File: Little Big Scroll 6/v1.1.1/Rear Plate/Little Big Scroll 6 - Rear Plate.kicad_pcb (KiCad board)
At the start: 2 copper layers, 59.2 x 87 mm, 6 parts

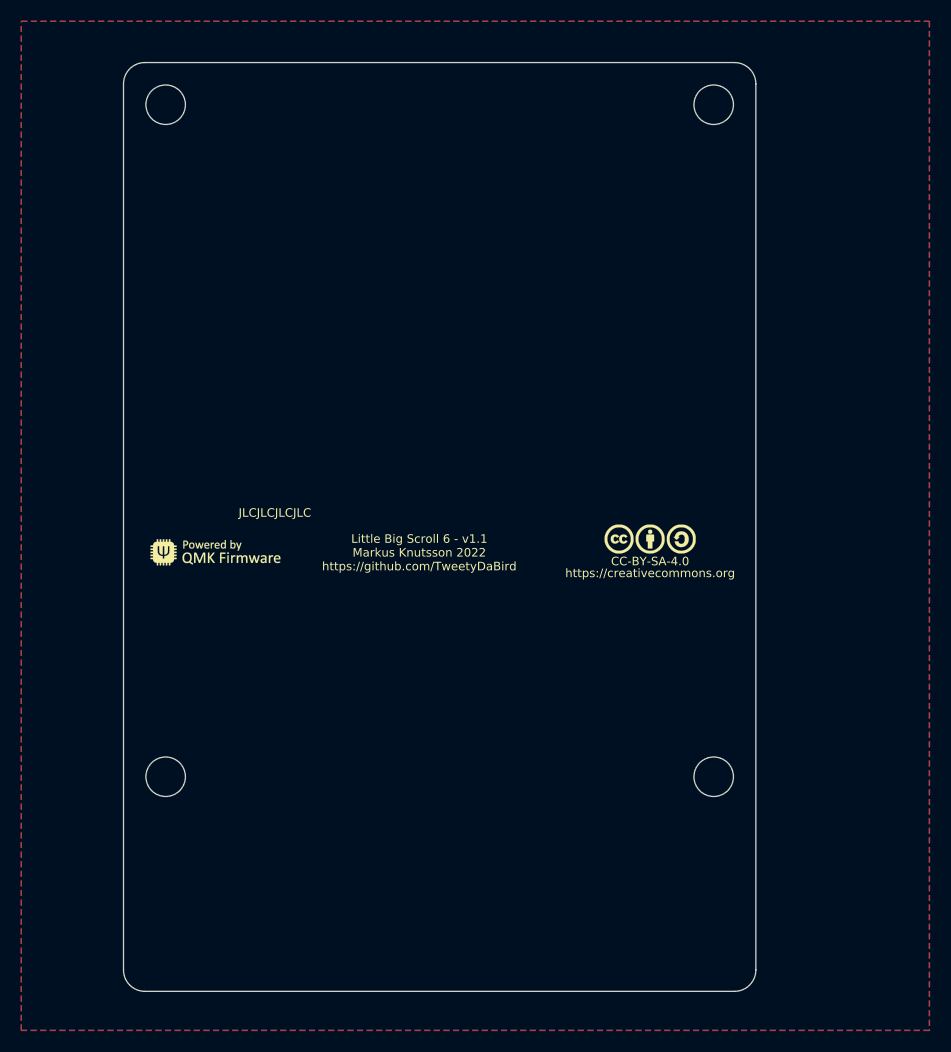
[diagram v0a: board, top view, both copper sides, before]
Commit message: LBS6 v1.1.1
Fixed plate holes
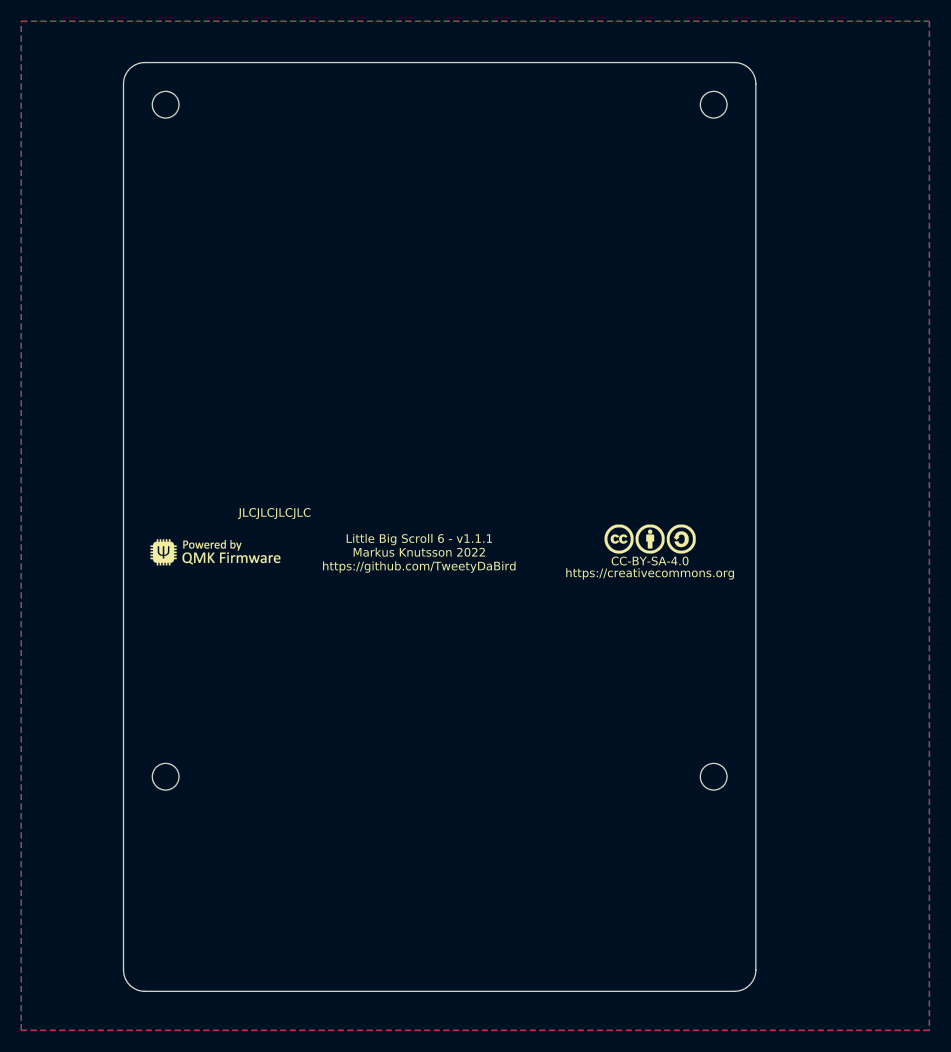
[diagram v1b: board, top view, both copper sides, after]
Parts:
- H1, H2, H3, H4: footprint Keyboard Switches & Encoders:Spacer PCB hole -> Keyboard_Plate:Spacer Plate hole
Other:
- board text added: "Little Big Scroll 6 - v1.1.1 Markus Knutsson 2022 https://github.com/TweetyDaBird"
- board text removed: "Little Big Scroll 6 - v1.1 Markus Knutsson 2022 https://github.com/TweetyDaBird"
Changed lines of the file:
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@@
   (title_block
     (title "Little Big Scroll 6 - Rear Plate")
-    (date "2022-08-26")
-    (rev "v1.1")
+    (date "2022-09-16")
+    (rev "v1.1.1")
     (company "Tweety's Wild Thinking")
     (comment 1 "Markus Knutsson <markus.knutsson@tweety.se>")
@@
   )
   (net 0 "")
-  (footprint "Keyboard Switches & Encoders:Spacer PCB hole" (layer "F.Cu")
+  (footprint "Keyboard_Plate:Spacer Plate hole" (layer "F.Cu")
     (at 84.6 112.685)
-    (descr "Mounting Hole 3.7mm, no annular")
-    (tags "mounting hole 3.7mm no annular")
+    (descr "Mounting Hole 2.5mm, no annular")
+    (tags "mounting hole 2.5mm no annular")
     (property "Sheetfile" "Little Big Scroll 6 - Rear Plate.kicad_sch")
     (property "Sheetname" "")
     (attr exclude_from_pos_files)
-    (fp_text reference "H1" (at 0 -4.7) (layer "F.SilkS") hide
+    (fp_text reference "H1" (at 0 -3.5) (layer "F.SilkS") hide
       (effects (font (size 1 1) (thickness 0.15)))
     )
-    (fp_text value "Spacer_PCB" (at 0 4.7) (layer "F.Fab") hide
+    (fp_text value "Spacer_PCB" (at 0 3.5) (layer "F.Fab")
       (effects (font (size 1 1) (thickness 0.15)))
     )
-    (fp_text user "${REFERENCE}" (at 0 0) (layer "F.Fab") hide
+    (fp_text user "${REFERENCE}" (at 0 0) (layer "F.Fab")
       (effects (font (size 1 1) (thickness 0.15)))
     )
-    (fp_circle (center 0 0) (end 3.7 0) (layer "Cmts.User") (width 0.15) (fill none))
-    (fp_circle (center 0 0) (end 3.95 0) (layer "F.CrtYd") (width 0.05) (fill none))
-    (pad "" np_thru_hole circle (at 0 0) (size 3.7 3.7) (drill 3.7) (layers *.Cu *.Mask))
+    (fp_circle (center 0 0) (end 2.5 0) (layer "Cmts.User") (width 0.15) (fill none))
+    (fp_circle (center 0 0) (end 2.75 0) (layer "F.CrtYd") (width 0.05) (fill none))
+    (pad "" np_thru_hole circle (at 0 0) (size 2.5 2.5) (drill 2.5) (layers *.Cu *.Mask))
   )
-  (footprint "Keyboard Switches & Encoders:Spacer PCB hole" (layer "F.Cu")
+  (footprint "Keyboard_Plate:Spacer Plate hole" (layer "F.Cu")
     (at 135.94 112.685)
-    (descr "Mounting Hole 3.7mm, no annular")
-    (tags "mounting hole 3.7mm no annular")
+    (descr "Mounting Hole 2.5mm, no annular")
+    (tags "mounting hole 2.5mm no annular")
     (property "Sheetfile" "Little Big Scroll 6 - Rear Plate.kicad_sch")
     (property "Sheetname" "")
     (attr exclude_from_pos_files)
-    (fp_text reference "H2" (at 0 -4.7) (layer "F.SilkS") hide
+    (fp_text reference "H2" (at 0 -3.5) (layer "F.SilkS") hide
       (effects (font (size 1 1) (thickness 0.15)))
     )
-    (fp_text value "Spacer_PCB" (at 0 4.7) (layer "F.Fab") hide
+    (fp_text value "Spacer_PCB" (at 0 3.5) (layer "F.Fab")
       (effects (font (size 1 1) (thickness 0.15)))
     )
-    (fp_text user "${REFERENCE}" (at 0 0) (layer "F.Fab") hide
+    (fp_text user "${REFERENCE}" (at 0 0) (layer "F.Fab")
       (effects (font (size 1 1) (thickness 0.15)))
     )
-    (fp_circle (center 0 0) (end 3.7 0) (layer "Cmts.User") (width 0.15) (fill none))
-    (fp_circle (center 0 0) (end 3.95 0) (layer "F.CrtYd") (width 0.05) (fill none))
-    (pad "" np_thru_hole circle (at 0 0) (size 3.7 3.7) (drill 3.7) (layers *.Cu *.Mask))
+    (fp_circle (center 0 0) (end 2.5 0) (layer "Cmts.User") (width 0.15) (fill none))
+    (fp_circle (center 0 0) (end 2.75 0) (layer "F.CrtYd") (width 0.05) (fill none))
+    (pad "" np_thru_hole circle (at 0 0) (size 2.5 2.5) (drill 2.5) (layers *.Cu *.Mask))
   )
-  (footprint "Keyboard Switches & Encoders:Spacer PCB hole" (layer "F.Cu")
+  (footprint "Keyboard_Plate:Spacer Plate hole" (layer "F.Cu")
     (at 135.94 49.73)
-    (descr "Mounting Hole 3.7mm, no annular")
-    (tags "mounting hole 3.7mm no annular")
+    (descr "Mounting Hole 2.5mm, no annular")
+    (tags "mounting hole 2.5mm no annular")
     (property "Sheetfile" "Little Big Scroll 6 - Rear Plate.kicad_sch")
     (property "Sheetname" "")
     (attr exclude_from_pos_files)
-    (fp_text reference "H3" (at 0 -4.7) (layer "F.SilkS") hide
+    (fp_text reference "H3" (at 0 -3.5) (layer "F.SilkS") hide
       (effects (font (size 1 1) (thickness 0.15)))
     )
-    (fp_text value "Spacer_PCB" (at 0 4.7) (layer "F.Fab") hide
+    (fp_text value "Spacer_PCB" (at 0 3.5) (layer "F.Fab")
       (effects (font (size 1 1) (thickness 0.15)))
     )
-    (fp_text user "${REFERENCE}" (at 0 0) (layer "F.Fab") hide
+    (fp_text user "${REFERENCE}" (at 0 0) (layer "F.Fab")
       (effects (font (size 1 1) (thickness 0.15)))
     )
-    (fp_circle (center 0 0) (end 3.7 0) (layer "Cmts.User") (width 0.15) (fill none))
-    (fp_circle (center 0 0) (end 3.95 0) (layer "F.CrtYd") (width 0.05) (fill none))
-    (pad "" np_thru_hole circle (at 0 0) (size 3.7 3.7) (drill 3.7) (layers *.Cu *.Mask))
+    (fp_circle (center 0 0) (end 2.5 0) (layer "Cmts.User") (width 0.15) (fill none))
+    (fp_circle (center 0 0) (end 2.75 0) (layer "F.CrtYd") (width 0.05) (fill none))
+    (pad "" np_thru_hole circle (at 0 0) (size 2.5 2.5) (drill 2.5) (layers *.Cu *.Mask))
   )
-  (footprint "Keyboard Switches & Encoders:Spacer PCB hole" (layer "F.Cu")
+  (footprint "Keyboard_Plate:Spacer Plate hole" (layer "F.Cu")
     (at 84.6 49.73)
-    (descr "Mounting Hole 3.7mm, no annular")
-    (tags "mounting hole 3.7mm no annular")
+    (descr "Mounting Hole 2.5mm, no annular")
+    (tags "mounting hole 2.5mm no annular")
     (property "Sheetfile" "Little Big Scroll 6 - Rear Plate.kicad_sch")
     (property "Sheetname" "")
     (attr exclude_from_pos_files)
-    (fp_text reference "H4" (at 0 -4.7) (layer "F.SilkS") hide
+    (fp_text reference "H4" (at 0 -3.5) (layer "F.SilkS") hide
       (effects (font (size 1 1) (thickness 0.15)))
     )
-    (fp_text value "Spacer_PCB" (at 0 4.7) (layer "F.Fab") hide
+    (fp_text value "Spacer_PCB" (at 0 3.5) (layer "F.Fab")
       (effects (font (size 1 1) (thickness 0.15)))
     )
-    (fp_text user "${REFERENCE}" (at 0 0) (layer "F.Fab") hide
+    (fp_text user "${REFERENCE}" (at 0 0) (layer "F.Fab")
       (effects (font (size 1 1) (thickness 0.15)))
     )
-    (fp_circle (center 0 0) (end 3.7 0) (layer "Cmts.User") (width 0.15) (fill none))
-    (fp_circle (center 0 0) (end 3.95 0) (layer "F.CrtYd") (width 0.05) (fill none))
-    (pad "" np_thru_hole circle (at 0 0) (size 3.7 3.7) (drill 3.7) (layers *.Cu *.Mask))
+    (fp_circle (center 0 0) (end 2.5 0) (layer "Cmts.User") (width 0.15) (fill none))
+    (fp_circle (center 0 0) (end 2.75 0) (layer "F.CrtYd") (width 0.05) (fill none))
+    (pad "" np_thru_hole circle (at 0 0) (size 2.5 2.5) (drill 2.5) (layers *.Cu *.Mask))
   )
   (footprint "Logotypes:Powered_by_QMK" (layer "F.Cu")
@@
   (gr_arc (start 139.89 130.789601) (mid 139.304097 132.204097) (end 137.889601 132.79) (layer "Edge.Cuts") (width 0.05))
   (gr_line (start 137.889601 132.79) (end 82.650399 132.790399) (layer "Edge.Cuts") (width 0.05))
-  (gr_text "Little Big Scroll 6 - v1.1\nMarkus Knutsson 2022\nhttps://github.com/TweetyDaBird" (at 108.361388 91.69) (layer "F.SilkS")
+  (gr_text "Little Big Scroll 6 - v1.1.1\nMarkus Knutsson 2022\nhttps://github.com/TweetyDaBird" (at 108.361388 91.69) (layer "F.SilkS")
     (effects (font (size 0.8 0.8) (thickness 0.15)))
   )
